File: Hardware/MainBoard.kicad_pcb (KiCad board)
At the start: 2 copper layers, 100 x 40 mm, 37 parts, among them J1 UPDI, J2 UART, J3 NMEA, J4 Vin, J5 TIME_ZONE, Q1 S8050, U1 HV5530, U2 HV5530, U3 ATtiny1606-S, U4 L78M05ABDT-TR

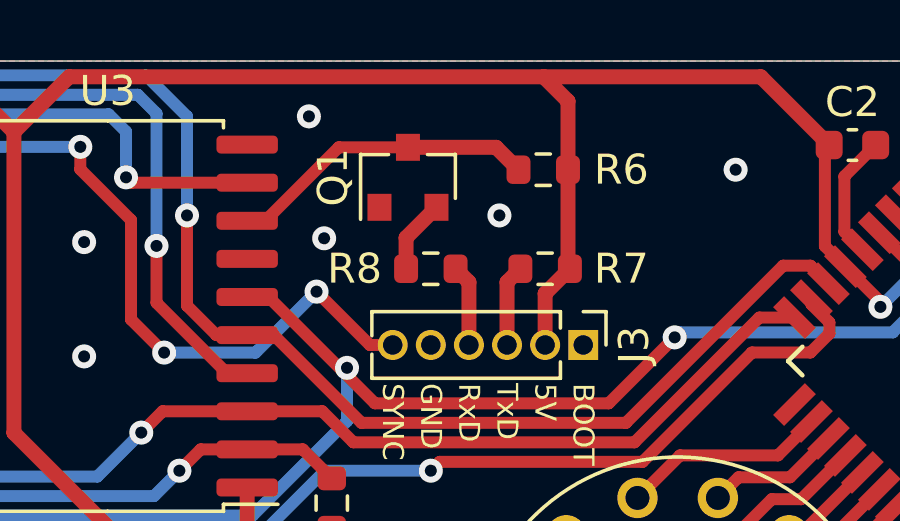
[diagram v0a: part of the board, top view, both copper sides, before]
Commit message: Fix Q1 pinout
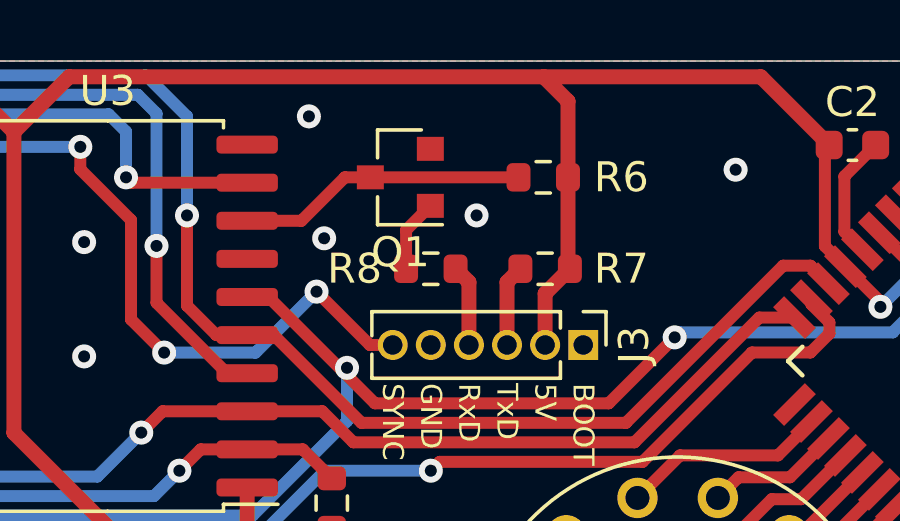
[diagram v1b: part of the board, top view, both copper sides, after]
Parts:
- moved Q1 0.25 mm to (79.8, 23.9), turned to 180 degrees
- moved R6 0.25 mm to (84.5, 23.9)
